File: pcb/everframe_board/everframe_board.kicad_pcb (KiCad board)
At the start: 2 copper layers, 0 parts

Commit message: Finished sch, started layout 2L only
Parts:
- added C1: 10uF, Capacitor_SMD:C_0805_2012Metric, B.Cu at (76.0, 64.6)
- added C10: 1uF, Capacitor_SMD:C_0603_1608Metric, B.Cu at (80.1, 78.2)
- added C11: 0.1uF, Capacitor_SMD:C_0603_1608Metric, B.Cu at (81.6, 78.2)
- added C12: 1uF, Capacitor_SMD:C_0603_1608Metric, B.Cu at (83.1, 78.2)
- added C13: 1uF, Capacitor_SMD:C_0603_1608Metric, F.Cu at (80.8, 81.8)
- added C14: 1uF, Capacitor_SMD:C_0603_1608Metric, F.Cu at (80.8, 83.8)
- added C15: 1uF, Capacitor_SMD:C_0603_1608Metric, B.Cu at (76.0, 81.0)
- added C16: 1uF, Capacitor_SMD:C_0603_1608Metric, B.Cu at (76.0, 82.5)
- added C17: 2.2uF, Capacitor_SMD:C_0603_1608Metric, B.Cu at (76.0, 78.0)
- added C18: 4.7uF, Capacitor_SMD:C_0805_2012Metric, F.Cu at (79.5, 57.0)
- added C19: 0.47uF, Capacitor_SMD:C_0805_2012Metric, F.Cu at (81.8, 57.0)
- added C2: 10uF, Capacitor_SMD:C_0805_2012Metric, B.Cu at (76.0, 66.6)
- added C20: 0.1uF, Capacitor_SMD:C_0603_1608Metric, F.Cu at (82.0, 61.7)
- added C21: 1uF, Capacitor_SMD:C_0603_1608Metric, F.Cu at (80.5, 61.7)
- added C22: 0.47uF, Capacitor_SMD:C_0603_1608Metric, F.Cu at (83.2, 84.8)
- added C23: 1uF, Capacitor_SMD:C_0603_1608Metric, B.Cu at (89.5, 90.5)
- added C24: 1uF, Capacitor_SMD:C_0603_1608Metric, B.Cu at (89.5, 84.5)
- added C25: 4.7uF, Capacitor_SMD:C_0805_2012Metric, F.Cu at (133.9, 111.0)
- added C26: 10uF, Capacitor_SMD:C_0805_2012Metric, F.Cu at (133.9, 114.0)
- added C27: 10uF, Capacitor_SMD:C_0805_2012Metric, F.Cu at (133.9, 117.0)
- added C28: 10uF, Capacitor_SMD:C_0805_2012Metric, F.Cu at (133.9, 120.0)
- added C29: 10uF, Capacitor_SMD:C_0805_2012Metric, F.Cu at (154.9, 109.1)
- added C3: 10uF, Capacitor_SMD:C_0805_2012Metric, B.Cu at (76.0, 68.6)
- added C30: 4.7uF, Capacitor_SMD:C_0805_2012Metric, F.Cu at (154.9, 112.1)
- added C31: 10uF, Capacitor_SMD:C_0805_2012Metric, F.Cu at (85.5, 125.0)
- added C32: 10uF, Capacitor_SMD:C_0805_2012Metric, F.Cu at (83.5, 125.0)
- added C33: 0.1uF, Capacitor_SMD:C_0603_1608Metric, F.Cu at (89.6, 113.8)
- added C34: 1uF, Capacitor_SMD:C_0603_1608Metric, F.Cu at (89.6, 115.3)
- added C35: 1uF, Capacitor_SMD:C_0603_1608Metric, B.Cu at (82.2, 119.4)
- added C4: 10uF, Capacitor_SMD:C_0805_2012Metric, B.Cu at (76.0, 70.6)
- added C5: 10uF, Capacitor_SMD:C_0805_2012Metric, B.Cu at (76.0, 72.6)
- added C6: 10uF, Capacitor_SMD:C_0805_2012Metric, B.Cu at (76.0, 74.6)
- added C7: 1uF, Capacitor_SMD:C_0603_1608Metric, F.Cu at (82.2, 71.0)
- added C8: 1uF, Capacitor_SMD:C_0603_1608Metric, F.Cu at (82.2, 72.5)
- added C9: 0.1uF, Capacitor_SMD:C_0603_1608Metric, B.Cu at (80.9, 80.5)
- added D1: MBR0530, Diode_SMD:D_SOD-123, F.Cu at (139.0, 111.2)
- added D2: MBR0530, Diode_SMD:D_SOD-123, F.Cu at (139.0, 114.5)
- added D3: MBR0530, Diode_SMD:D_SOD-123, F.Cu at (139.0, 117.8)
- added D4: MBR0530, Diode_SMD:D_SOD-123, F.Cu at (160.0, 117.5)
- added D5: PESD5V0L1ULD, Diode_SMD:D_SOD-882D, F.Cu at (84.6, 129.4)
- added FB1: 30mOhm@100MHz, Inductor_SMD:L_0603_1608Metric, F.Cu at (84.5, 127.5)
- added H1: MountingHole, MountingHole:MountingHole_2mm, F.Cu at (75.0, 52.0)
- added H2: MountingHole, MountingHole:MountingHole_2mm, F.Cu at (91.0, 52.0)
- added H3: MountingHole, MountingHole:MountingHole_2mm, F.Cu at (75.0, 136.0)
- added H4: MountingHole, MountingHole:MountingHole_2mm, F.Cu at (91.0, 136.0)
- added J1: 62684-501100ALF, everframe_library.footprints:AMPHENOL_62684-501100ALF, F.Cu at (73.7, 73.0)
- added J2: GSB1CA11101DSHR, everframe_library.footprints:AMPHENOL_GSB1CA11101DSHR, F.Cu at (77.1, 128.1)
- added L1: 10uH, Inductor_SMD:L_1008_2520Metric, F.Cu at (138.6, 121.4)
- added L2: 10uH, Inductor_SMD:L_1008_2520Metric, F.Cu at (159.6, 114.0)
- added Q1: BSS138, Package_TO_SOT_SMD:SOT-23, F.Cu at (143.5, 121.8)
- added Q2: SI2301CDS-T1-E3, Package_TO_SOT_SMD:SOT-23, F.Cu at (159.5, 109.8)
- added R1: 0, Resistor_SMD:R_0603_1608Metric, F.Cu at (89.0, 60.0)
- added R10: 0.47, Resistor_SMD:R_0603_1608Metric, F.Cu at (143.9, 110.7)
- added R11: 1M, Resistor_SMD:R_0603_1608Metric, F.Cu at (143.9, 113.2)
- added R12: 0.47, Resistor_SMD:R_0603_1608Metric, F.Cu at (143.9, 115.8)
- added R13: 1M, Resistor_SMD:R_0603_1608Metric, F.Cu at (154.6, 114.9)
- added R14: 0.47, Resistor_SMD:R_0603_1608Metric, F.Cu at (154.6, 117.4)
- added R15: 5.1k, Resistor_SMD:R_0603_1608Metric, B.Cu at (75.1, 123.0)
- added R16: 5.1k, Resistor_SMD:R_0603_1608Metric, F.Cu at (81.5, 125.0)
- added R17: 33, Resistor_SMD:R_0603_1608Metric, B.Cu at (79.5, 91.0)
- added R18: 33, Resistor_SMD:R_0603_1608Metric, B.Cu at (78.0, 91.0)
- added R19: 33, Resistor_SMD:R_0603_1608Metric, B.Cu at (76.5, 91.0)
- added R2: 0, Resistor_SMD:R_0603_1608Metric, F.Cu at (89.0, 57.0)
- added R20: 100k, Resistor_SMD:R_0603_1608Metric, F.Cu at (78.0, 91.0)
- added R21: 1k, Resistor_SMD:R_0603_1608Metric, B.Cu at (80.6, 119.4)
- added R22: 0, Resistor_SMD:R_0603_1608Metric, B.Cu at (75.0, 91.0)
- added R23: 0, Resistor_SMD:R_0603_1608Metric, F.Cu at (75.0, 91.0)
- added R24: 0, Resistor_SMD:R_0603_1608Metric, F.Cu at (76.5, 91.0)
- added R25: 0, Resistor_SMD:R_0603_1608Metric, F.Cu at (79.5, 91.0)
- added R26: 0, Resistor_SMD:R_0603_1608Metric, F.Cu at (81.0, 91.0)
- added R3: 0, Resistor_SMD:R_0603_1608Metric, F.Cu at (90.5, 60.0)
- added R4: 0, Resistor_SMD:R_0603_1608Metric, F.Cu at (90.5, 57.0)
- added R5: 0, Resistor_SMD:R_0603_1608Metric, F.Cu at (81.3, 59.5)
- added R6: 0, Resistor_SMD:R_0603_1608Metric, F.Cu at (80.8, 85.5)
- added R7: 100k, Resistor_SMD:R_0603_1608Metric, B.Cu at (86.2, 88.0)
- added R8: 0, Resistor_SMD:R_0603_1608Metric, B.Cu at (86.7, 90.5)
- added R9: 0, Resistor_SMD:R_0603_1608Metric, B.Cu at (85.2, 90.5)
- added SW1: SW_Push, Button_Switch_SMD:SW_Push_1P1T_NO_CK_KMR2, F.Cu at (77.0, 118.0)
- added TP1: TestPoint, TestPoint:TestPoint_Pad_2.0x2.0mm, F.Cu at (183.3, 106.0)
- added TP10: TestPoint, TestPoint:TestPoint_Pad_2.0x2.0mm, F.Cu at (195.5, 106.0)
- added TP11: TestPoint, TestPoint:TestPoint_Pad_2.0x2.0mm, F.Cu at (195.5, 110.0)
- added TP12: TestPoint, TestPoint:TestPoint_Pad_2.0x2.0mm, F.Cu at (195.5, 114.1)
- added TP2: TestPoint, TestPoint:TestPoint_Pad_2.0x2.0mm, F.Cu at (183.3, 110.0)
- added TP3: TestPoint, TestPoint:TestPoint_Pad_2.0x2.0mm, F.Cu at (183.3, 114.1)
- added TP4: TestPoint, TestPoint:TestPoint_Pad_2.0x2.0mm, F.Cu at (187.4, 106.0)
- added TP5: TestPoint, TestPoint:TestPoint_Pad_2.0x2.0mm, F.Cu at (187.4, 110.0)
- added TP6: TestPoint, TestPoint:TestPoint_Pad_2.0x2.0mm, F.Cu at (187.4, 114.1)
- added TP7: TestPoint, TestPoint:TestPoint_Pad_2.0x2.0mm, F.Cu at (191.4, 106.0)
- added TP8: TestPoint, TestPoint:TestPoint_Pad_2.0x2.0mm, F.Cu at (191.4, 110.0)
- added TP9: TestPoint, TestPoint:TestPoint_Pad_2.0x2.0mm, F.Cu at (191.4, 114.1)
- added U1: MODULE-SEEEDUINO-XIAO-ESP32S3, everframe_library.footprints:MOUDLE14P-SMD-2.54-21X17.8MM, F.Cu at (72.4, 94.1)
- added U2: TLV75533PDBV, Package_TO_SOT_SMD:SOT-23-5, B.Cu at (89.5, 87.5)
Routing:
- net /epaper display (page 3)/RST_N: track 0.00 -> 40.8 mm, vias 0 -> 1
- net /epaper display (page 3)/DC: track 0.00 -> 34.6 mm, vias 0 -> 1
- net /epaper display (page 3)/CS: track 0.00 -> 32.6 mm
- net /epaper display (page 3)/BUSY_N: track 0.00 -> 30.7 mm
- net /epaper display (page 3)/SCK: track 0.00 -> 29.5 mm, vias 0 -> 1
- net /epaper display (page 3)/SI1: track 0.00 -> 27.7 mm, vias 0 -> 1
- net /epaper display (page 3)/SI0: track 0.00 -> 25.9 mm, vias 0 -> 1
- net /esp32-s3/ESP32_MOSI: track 0.00 -> 24.7 mm, vias 0 -> 1
- net /esp32-s3/ESP32_SCK: track 0.00 -> 24.5 mm, vias 0 -> 1
- net /esp32-s3/ESP32_MISO: track 0.00 -> 24.0 mm, vias 0 -> 1
- net /esp32-s3/ESP32_DC: track 0.00 -> 23.6 mm, vias 0 -> 1
- net GND: track 0.00 -> 19.2 mm, vias 0 -> 41
- net +3V3_ESP32: track 0.00 -> 16.7 mm
- net /epaper display (page 3)/BS1: track 0.00 -> 11.4 mm
- net /epaper display (page 3)/BS0: track 0.00 -> 11.0 mm
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- added copper zone on B.Cu, net +5V_USB
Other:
- board outline added: 22 x 90 mm

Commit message: Routed board, mostly need checks
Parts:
- removed TP1, TP10, TP11, TP12, TP2, TP3, TP4, TP5, TP6, TP7, TP8, TP9: TestPoint, TestPoint:TestPoint_Pad_2.0x2.0mm
- added J3: SM02B-GHS-TB, Connector_JST:JST_GH_SM02B-GHS-TB_1x02-1MP_P1.25mm_Horizontal, F.Cu at (90.5, 129.0)
- C29, C30, D4, L2, Q2, R13, R14: moved to B.Cu
- U1: value MODULE-SEEEDUINO-XIAO-ESP32S3 -> XIAO-ESP32-S3-SMD; footprint everframe_library.footprints:MOUDLE14P-SMD-2.54-21X17.8MM -> seed_studio:XIAO-ESP32S3-SMD
- moved Q2 95.0 mm to (83.3, 53.2), turned to 90 degrees
- moved C30 94.8 mm to (80.4, 53.4), turned to 90 degrees
- moved D4 94.5 mm to (85.3, 59.6)
- moved L2 93.5 mm to (85.7, 56.7), turned to 180 degrees
- moved R13 92.0 mm to (86.0, 53.6), turned to 90 degrees
- moved R14 89.1 mm to (89.4, 56.7), turned to 180 degrees
- moved Q1 83.6 mm to (87.1, 60.0), turned to -90 degrees
- moved C29 82.0 mm to (89.6, 59.5), turned to 180 degrees
- moved R11 79.8 mm to (87.2, 57.1)
- moved R10 79.5 mm to (84.2, 58.2), turned to -90 degrees
- moved L1 79.4 mm to (90.4, 58.3), turned to -90 degrees
- moved R12 73.4 mm to (86.2, 70.3)
- moved C25 72.7 mm to (87.4, 55.0)
- moved C28 72.4 mm to (91.3, 61.4), turned to 180 degrees
- moved D3 72.4 mm to (89.5, 65.0), turned to 90 degrees
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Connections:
- J1 pad 13: /epaper display (page 3)/VGH -> /epaper display (page 3)/VGL
- J1 pad 24: /epaper display (page 3)/TSCL -> unconnected-(J1-Pad24)
- J1 pad 25: /epaper display (page 3)/TSDA -> unconnected-(J1-Pad25)
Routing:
- net /esp32-s3/VBAT: track 0.00 -> 33.0 mm, vias 0 -> 3
- net Net-(U1-GPIO1_A0_D0): track 1.62 -> 31.2 mm, vias 0 -> 3
- net +5V: track 4.28 -> 33.5 mm, vias 3 -> 4
- net +3.3V: track 9.42 -> 37.8 mm, vias 5 -> 14
- net /epaper display (page 3)/VGH: track 0.00 -> 27.5 mm, vias 0 -> 5
- net /epaper display (page 3)/GDRC: track 2.22 -> 27.0 mm, vias 0 -> 3
- net GND: track 19.2 -> 41.0 mm, vias 41 -> 49
- net /epaper display (page 3)/RESEC: track 2.62 -> 17.1 mm, vias 0 -> 1
- net /epaper display (page 3)/GDRH: track 3.40 -> 16.4 mm, vias 1 -> 2
- net /epaper display (page 3)/RESEH: track 0.00 -> 13.0 mm
- net /epaper display (page 3)/VPC: track 2.86 -> 14.6 mm, vias 0 -> 1
- net /epaper display (page 3)/VPH: track 0.00 -> 10.1 mm
- net /epaper display (page 3)/BS0: track 11.0 -> 17.2 mm
- net /epaper display (page 3)/BS1: track 11.4 -> 16.0 mm
- net Net-(D2-K): track 0.00 -> 4.48 mm
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- added copper zone on B.Cu, net +3.3V
- added copper zone on F.Cu, net +3.3V
- added copper zone on F.Cu, net +5V
- added copper zone on F.Cu, net +5V_USB
- added copper zone on B.Cu, net GND
- added copper zone on F.Cu, net GND
- added copper zone on F.Cu, net Net-(D1-A)
- added copper zone on B.Cu, net Net-(D4-K)
- removed copper zone on B.Cu, net +5V_USB
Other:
- outline, holes or cut-outs redrawn

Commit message: Update pcb and create packaging design
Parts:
- moved C6 0.30 mm to (76.0, 74.9)
- moved C5 0.20 mm to (76.0, 72.8)
- moved R22 0.20 mm to (74.8, 91.0)
- moved R23 0.20 mm to (74.8, 91.0)
- moved R26 0.20 mm to (81.2, 91.0)
- moved C1 0.20 mm to (76.0, 64.4), turned to 0 degrees
- moved R2 0.13 mm to (92.4, 74.3)
- moved C20 0.11 mm to (82.1, 61.8)
- moved C21 0.11 mm to (80.5, 61.8)
- moved R1 0.10 mm to (92.4, 77.4)
- moved C12 0.10 mm to (83.2, 78.2)
- moved C4 0.10 mm to (76.0, 70.7)
- moved R9 0.10 mm to (85.1, 90.5)
- moved C10 0.10 mm to (80.0, 78.2)
- moved C16 0.10 mm to (76.0, 82.6)
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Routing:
- net +5V: track 33.5 -> 9.84 mm, vias 4 -> 14
- net /epaper display (page 3)/VGL: track 1.87 -> 17.8 mm
- net +3.3V: track 37.8 -> 22.9 mm, vias 14 -> 23
- net /epaper display (page 3)/VSL_LV2: track 0.00 -> 9.17 mm, vias 0 -> 1
- net /epaper display (page 3)/VSL: track 4.98 -> 9.02 mm
- net /epaper display (page 3)/VSH: track 3.47 -> 7.49 mm, vias 0 -> 1
- net /epaper display (page 3)/VPH: track 10.1 -> 13.9 mm
- net /epaper display (page 3)/VSH_LV2: track 4.30 -> 7.90 mm
- net /epaper display (page 3)/VSL_LV: track 5.62 -> 8.94 mm
- net /esp32-s3/VBAT: track 33.0 -> 36.2 mm, vias 3 -> 6
- net GND: track 41.0 -> 43.4 mm, vias 49 -> 144
- net +5V_USB: track 11.2 -> 9.49 mm, vias 5 -> 6
- net /epaper display (page 3)/VSH_LV: track 7.36 -> 6.09 mm
- net /epaper display (page 3)/VGH: vias 5 -> 4
- added copper zone on In1.Cu, net +3.3V
- added copper zone on B.Cu, net +5V
- added copper zone on In1.Cu, net +5V
- added copper zone on In1.Cu, net +5V_USB
- added copper zone on In1.Cu, net GND
- added copper zone on In2.Cu, net GND
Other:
- copper layers 2 -> 4

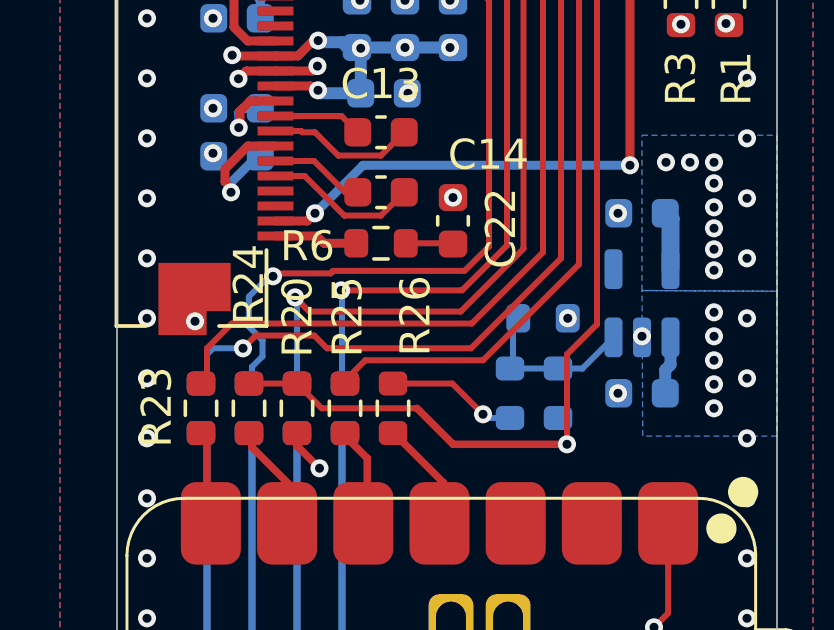
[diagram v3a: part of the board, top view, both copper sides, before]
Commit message: Some unused google cloud function code added, esp32 idf embedded project added with display drivers, pcb fab exported
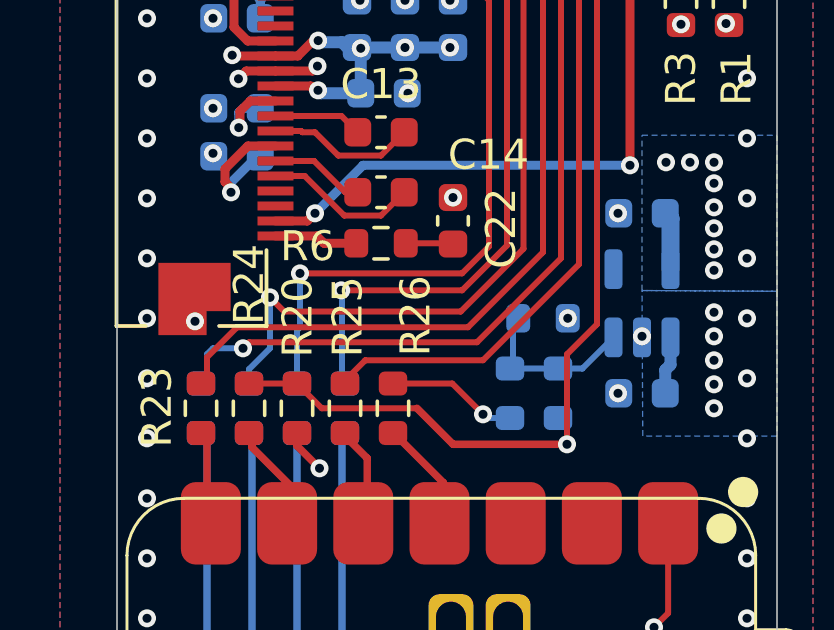
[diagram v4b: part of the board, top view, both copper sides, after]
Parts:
- R12: value 0.47 -> 0
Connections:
- R18 pad 1: /esp32-s3/ESP32_SCK -> /esp32-s3/ESP32_MISO
- R18 pad 2: /epaper display (page 3)/SCK -> /epaper display (page 3)/SI1
- R19 pad 1: /esp32-s3/ESP32_MISO -> /esp32-s3/ESP32_SCK
- R19 pad 2: /epaper display (page 3)/SI1 -> /epaper display (page 3)/SCK
- U1 pad 10: /esp32-s3/ESP32_SCK -> /esp32-s3/ESP32_MISO
- U1 pad 9: /esp32-s3/ESP32_MISO -> /esp32-s3/ESP32_SCK
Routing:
- net /epaper display (page 3)/SI1: track 27.7 -> 26.1 mm
- net /epaper display (page 3)/SCK: track 29.5 -> 30.6 mm
